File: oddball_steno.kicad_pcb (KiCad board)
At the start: 2 copper layers, 135.9 x 132.1 mm, 83 parts, among them J2 Conn_01x04, J3 Conn_02x04_Counter_Clockwise, J4 Conn_01x04, J5 Conn_01x04, J6 Conn_01x04, SW1 SW_SPST, SW2 SW_SPST, U1 Elite-C, U2 TRRS, U3 Elite-C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

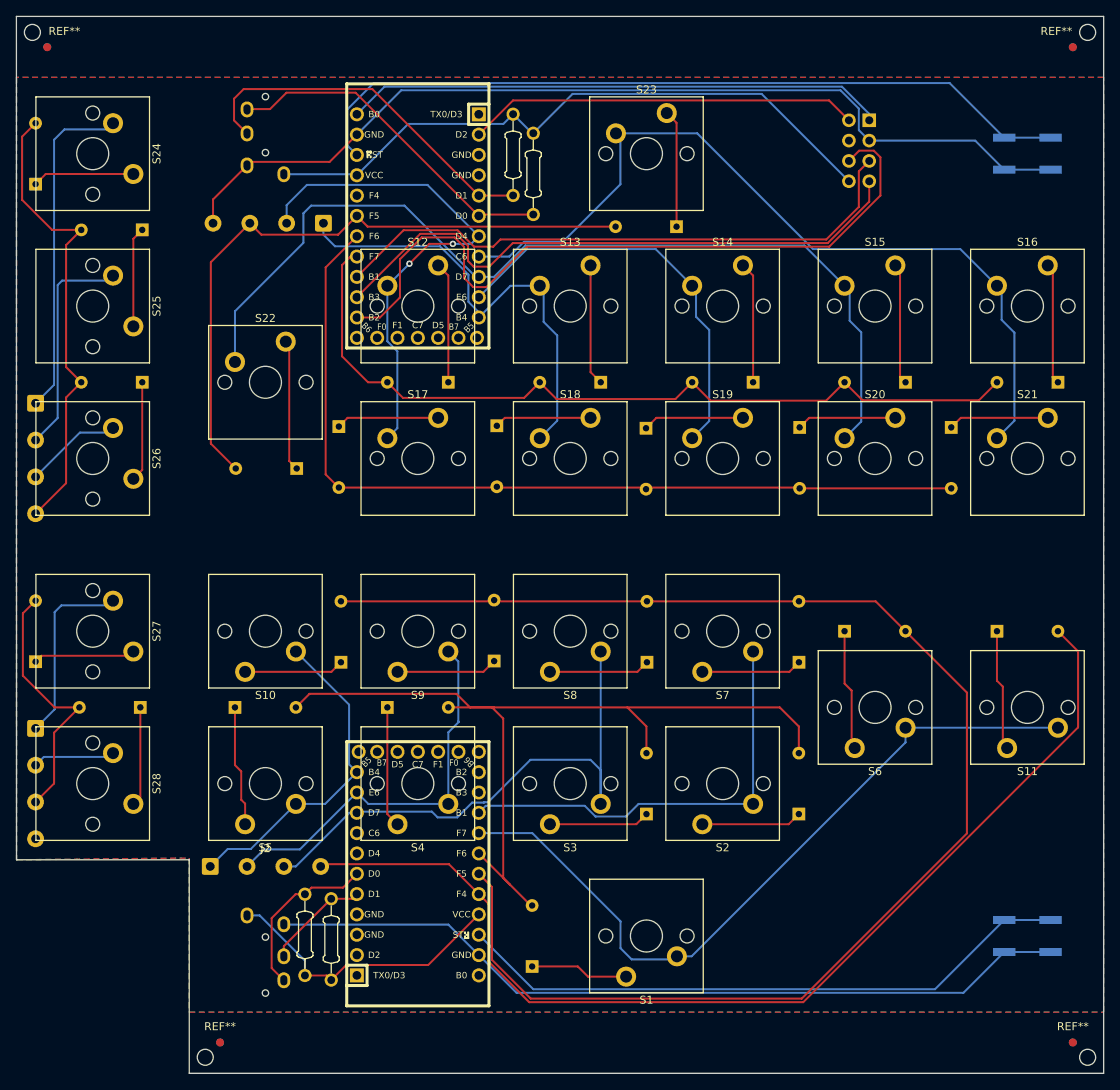
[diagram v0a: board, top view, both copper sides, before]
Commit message: Make v-cut lines .15mm
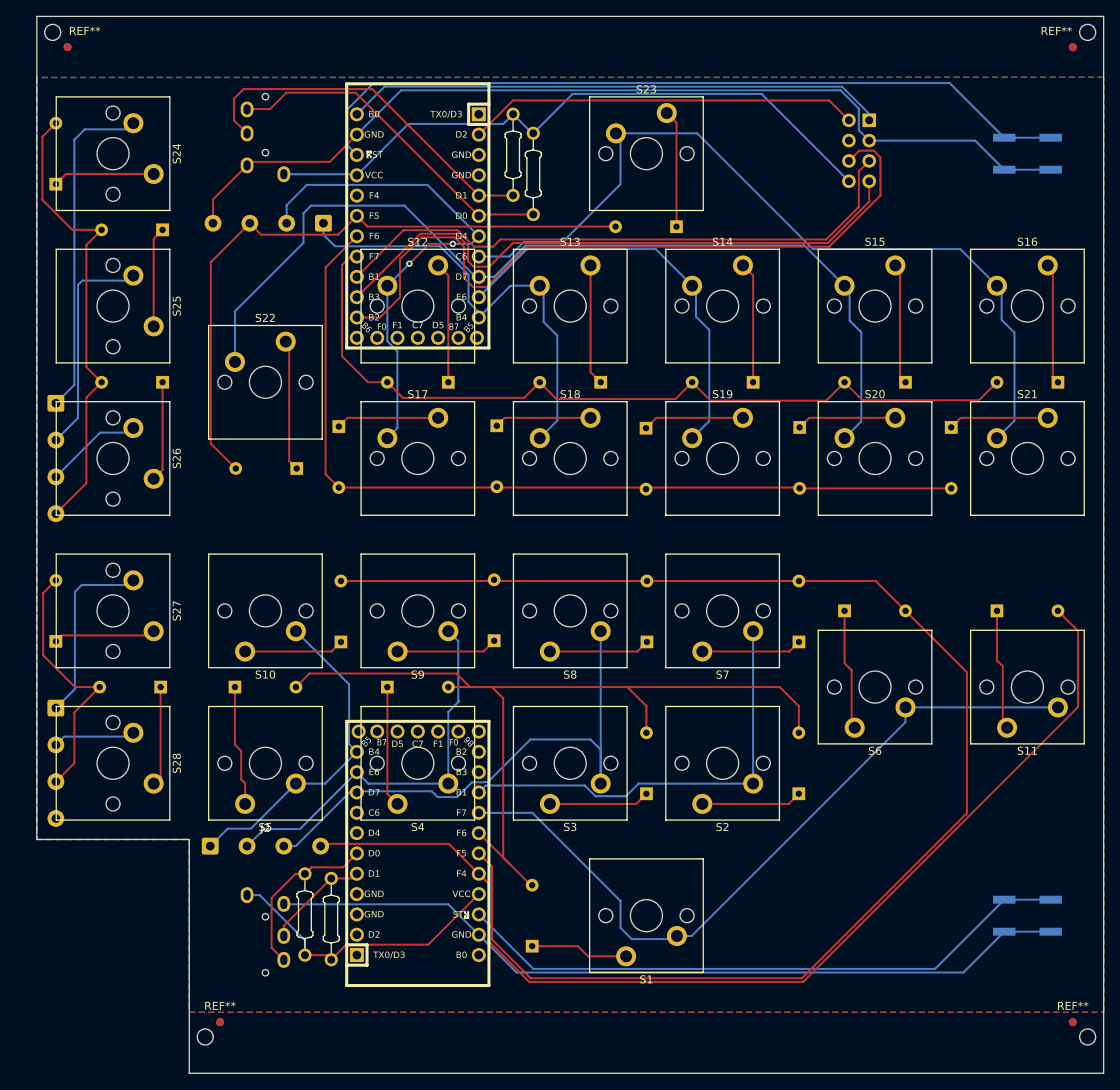
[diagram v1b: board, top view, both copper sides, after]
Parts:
- moved D28 3.59 mm to (91.8, 103.3)
- moved J6 3.59 mm to (78.7, 105.9)
- moved D27 3.59 mm to (78.7, 97.5)
- moved S28 3.59 mm to (85.9, 112.8)
- moved S27 3.59 mm to (85.9, 93.7)
- moved R4 2.54 mm to (109.8, 131.7)
- moved U2 2.54 mm to (104.9, 140.6)
- moved ? 2.54 mm to (78.3, 21.4)
- moved D10 2.54 mm to (114.3, 97.6)
- moved D24 2.54 mm to (78.7, 40.4)
- moved D4 2.54 mm to (120.1, 103.3)
- moved D5 2.54 mm to (101.1, 103.3)
- moved D7 2.54 mm to (171.6, 97.6)
- moved D8 2.54 mm to (152.6, 97.6)
- moved J5 2.54 mm to (78.7, 67.8)
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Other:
- board size 135.9 x 132.1 mm -> 133.3 x 132.1 mm
